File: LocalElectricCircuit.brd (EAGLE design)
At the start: 160 x 100 mm, 46 parts, among them IC1 PIC32MX360F512L, J1 Prog. Port, J3 Prog. Port, T1 PN100, U1 ADS1118, U2 ADS1118

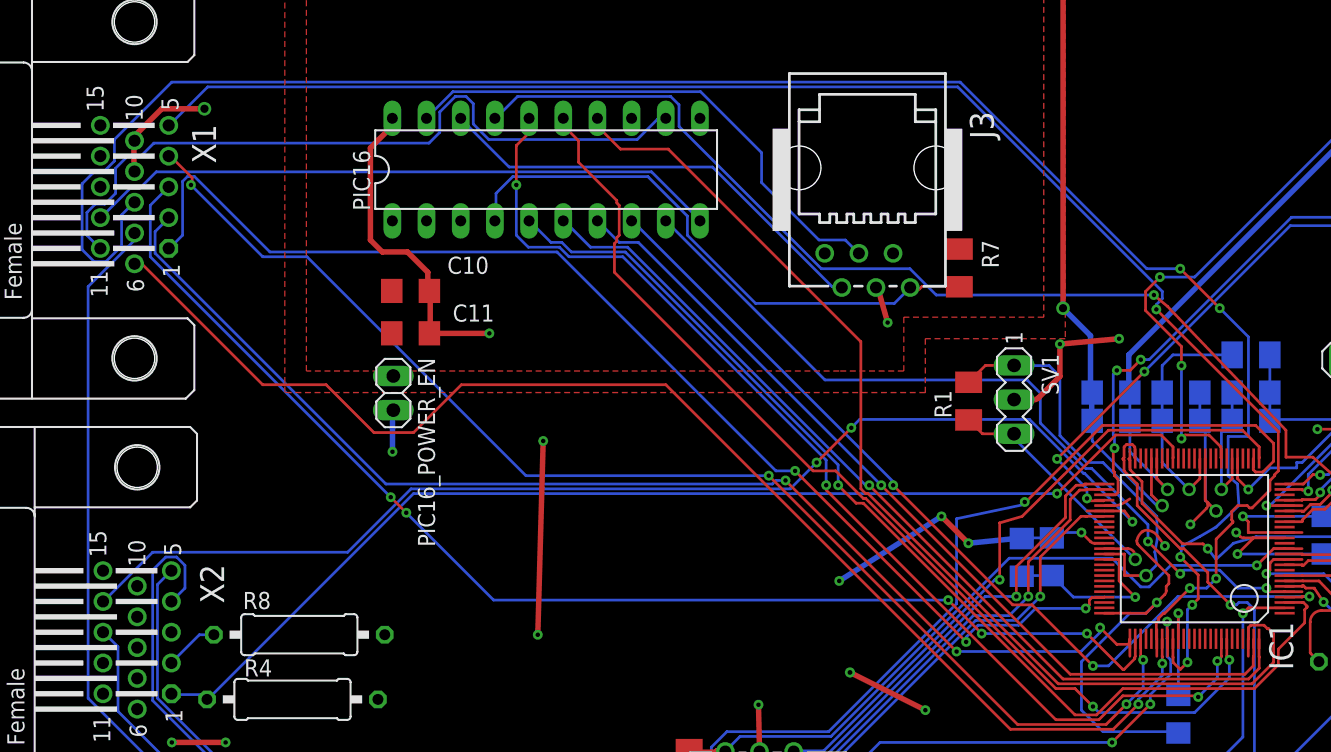
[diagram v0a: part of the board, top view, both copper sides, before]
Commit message: So far I've only ripped up a trace to have something to commit for the new branch
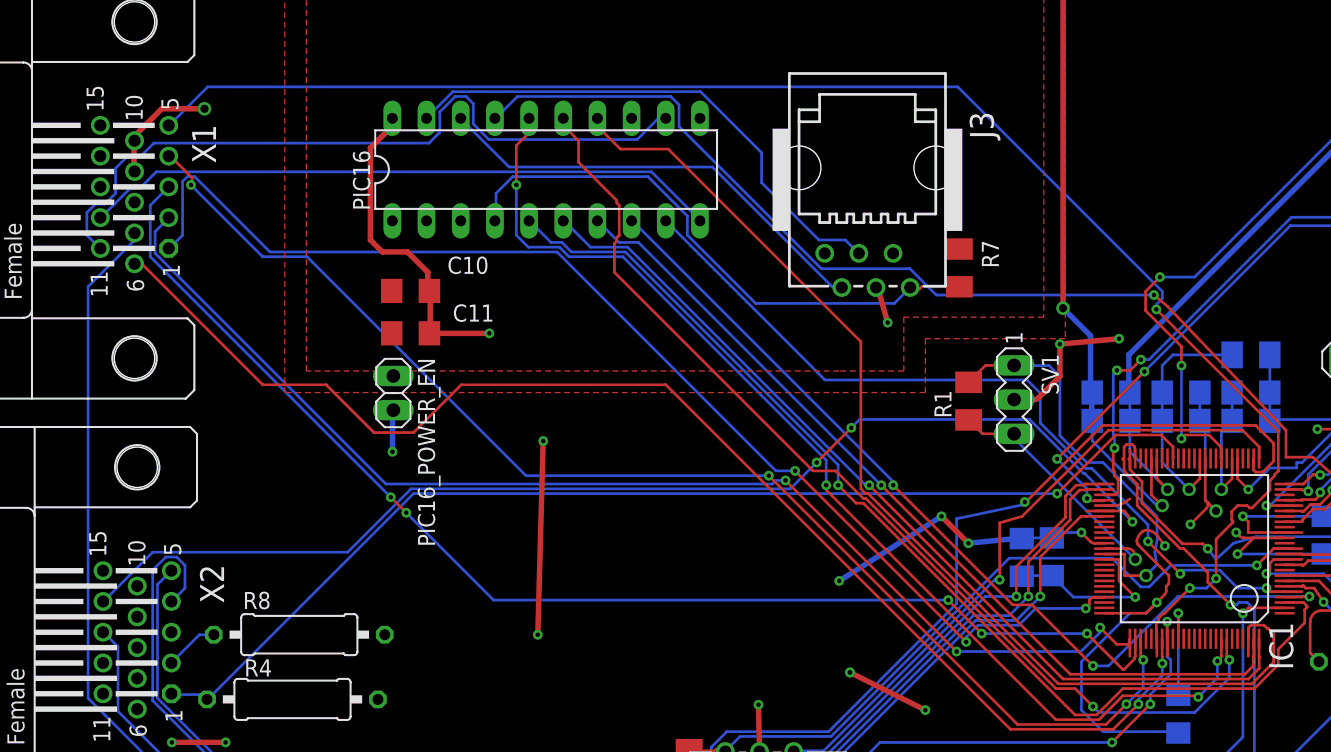
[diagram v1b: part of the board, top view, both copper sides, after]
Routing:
- net BALLC2: track 143.3 -> 0.00 mm, vias 5 -> 0
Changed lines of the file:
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@@
 <contactref element="IC1" pad="84"/>
 <contactref element="X1" pad="8"/>
-<wire x1="88.8" y1="-5.1" x2="88.8" y2="-6.4" width="0.2032" layer="1"/>
-<wire x1="88.8111" y1="-6.8453" x2="88.8111" y2="-6.4897" width="0.2032" layer="1"/>
-<wire x1="89.3445" y1="-7.3787" x2="88.8111" y2="-6.8453" width="0.2032" layer="1"/>
-<wire x1="89.8779" y1="-6.8453" x2="89.3445" y2="-7.3787" width="0.2032" layer="1"/>
-<wire x1="89.8779" y1="-2.9337" x2="89.8779" y2="-6.8453" width="0.2032" layer="16"/>
-<wire x1="90.2335" y1="-2.5781" x2="89.8779" y2="-2.9337" width="0.2032" layer="16"/>
-<wire x1="90.678" y1="-2.1336" x2="90.2335" y2="-2.5781" width="0.2032" layer="1"/>
-<wire x1="90.678" y1="-0.3556" x2="90.678" y2="-2.1336" width="0.2032" layer="1"/>
-<wire x1="89.3445" y1="0.9779" x2="90.678" y2="-0.3556" width="0.2032" layer="1"/>
-<wire x1="89.4779" y1="1.7779" x2="89.3445" y2="0.9779" width="0.2032" layer="16"/>
-<wire x1="93.7006" y1="4.8006" x2="92" y2="3.2" width="0.2032" layer="16"/>
-<wire x1="92" y1="3.2" x2="90.8" y2="2.5" width="0.2032" layer="16"/>
-<wire x1="90.8" y1="2.5" x2="89.4779" y2="1.7779" width="0.2032" layer="16"/>
-<wire x1="92.90431875" y1="9.934440625" x2="92.9" y2="7" width="0.2032" layer="16"/>
-<wire x1="92.9" y1="7" x2="93.6" y2="6.4" width="0.2032" layer="16"/>
-<wire x1="93.6" y1="6.4" x2="93.7006" y2="4.8006" width="0.2032" layer="16"/>
-<wire x1="94.4118" y1="9.936340625" x2="92.90431875" y2="9.934440625" width="0.2032" layer="16"/>
-<wire x1="94.4118" y1="17.3355" x2="94.4118" y2="9.936340625" width="0.2032" layer="16"/>
-<wire x1="92.2782" y1="19.4691" x2="94.4118" y2="17.3355" width="0.2032" layer="16"/>
-<wire x1="89.3445" y1="22.4028" x2="92.2782" y2="19.4691" width="0.2032" layer="1"/>
-<wire x1="86.8553" y1="22.4028" x2="89.3445" y2="22.4028" width="0.2032" layer="16"/>
-<wire x1="72.9869" y1="36.2712" x2="86.8553" y2="22.4028" width="0.2032" layer="16"/>
-<wire x1="14.4018" y1="36.2712" x2="72.9869" y2="36.2712" width="0.2032" layer="16"/>
-<wire x1="10.1346" y1="32.004" x2="14.4018" y2="36.2712" width="0.2032" layer="16"/>
-<wire x1="10.1346" y1="30.4038" x2="10.1346" y2="32.004" width="0.2032" layer="16"/>
-<wire x1="9.3345" y1="29.6037" x2="10.1346" y2="30.4038" width="0.2032" layer="16"/>
-<wire x1="8.6233" y1="29.6037" x2="9.3345" y2="29.6037" width="0.2032" layer="16"/>
-<wire x1="7.7343" y1="28.7147" x2="8.6233" y2="29.6037" width="0.2032" layer="16"/>
-<wire x1="7.7343" y1="23.8252" x2="7.7343" y2="28.7147" width="0.2032" layer="16"/>
-<wire x1="8.6233" y1="22.9362" x2="7.7343" y2="23.8252" width="0.2032" layer="16"/>
-<wire x1="9.5123" y1="22.9362" x2="8.6233" y2="22.9362" width="0.2032" layer="16"/>
-<wire x1="10.668" y1="24.0919" x2="9.5123" y2="22.9362" width="0.2032" layer="16"/>
-<wire x1="10.668" y1="26.4033" x2="10.668" y2="24.0919" width="0.2032" layer="16"/>
-<wire x1="11.557" y1="27.2923" x2="10.668" y2="26.4033" width="0.2032" layer="16"/>
-<wire x1="88.8111" y1="-6.4897" x2="88.8" y2="-6.4" width="0.2032" layer="1"/>
-<wire x1="11.557" y1="27.2923" x2="11.63" y2="27.342" width="0.2032" layer="16"/>
-<via x="89.8779" y="-6.8453" extent="1-16" drill="0.3302"/>
-<via x="90.2335" y="-2.5781" extent="1-16" drill="0.3302"/>
-<via x="89.3445" y="0.9779" extent="1-16" drill="0.3302"/>
-<via x="92.2782" y="19.4691" extent="1-16" drill="0.3302"/>
-<via x="89.3445" y="22.4028" extent="1-16" drill="0.3302"/>
+<wire x1="11.63" y1="27.342" x2="88.8" y2="-5.1" width="0" layer="19" extent="1-1"/>
 </signal>
 <signal name="BALLS1">

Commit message: Fan out step numero uno
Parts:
- removed PIC32_POWER_EN: (no value), pinhead:1X02
- moved C16 138.7 mm to (215.8, -26.2)
- moved C6 138.7 mm to (213.6, -26.3)
- moved C12 132.0 mm to (212.2, -21.3)
- moved C4 132.0 mm to (212.2, -19.2)
- moved C14 131.6 mm to (217.0, -21.3)
- moved C5 131.6 mm to (217.0, -19.2)
- moved C17 131.3 mm to (221.8, -21.3)
- moved C3 131.3 mm to (221.8, -19.2)
- moved R2 130.9 mm to (218.0, -27.8), turned to 270 degrees
- moved SV1 130.7 mm to (204.2, -17.3)
- moved IC1 130.7 mm to (217.6, -28.4)
- moved R1 130.7 mm to (200.8, -17.4)
- moved C1 128.1 mm to (217.4, -34.6)
- moved C15 128.1 mm to (217.4, -32.4)
- moved C7 126.8 mm to (214.0, -33.1)
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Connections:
- net +3V3: no longer PIC32_POWER_EN.1, PIC32_POWER_EN.2
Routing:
- net GND_3V3: track 258.8 -> 78.8 mm, vias 23 -> 6
- net BALLC1: track 131.4 -> 4.03 mm, vias 3 -> 1
- net U2TX: track 122.3 -> 0.00 mm, vias 3 -> 0
- net BALLA3: track 117.9 -> 3.70 mm, vias 3 -> 1
- net +3V3: track 197.4 -> 87.8 mm, vias 10 -> 6
- net U2RX: track 110.9 -> 4.03 mm, vias 1 -> 0
- net I_2_H: track 105.6 -> 4.90 mm, vias 3 -> 1
- net U1RX: track 102.4 -> 4.83 mm, vias 1 -> 0
- net BALLA4: track 98.2 -> 3.87 mm, vias 2 -> 1
- net BALLA2: track 95.3 -> 3.87 mm, vias 4 -> 1
- net GND_5V: track 91.3 -> 0.00 mm, vias 2 -> 0
- net U1TX: track 95.9 -> 4.67 mm, vias 1 -> 0
- net BALLS1: track 90.2 -> 0.00 mm, vias 3 -> 0
- net BALLA1: track 93.4 -> 3.70 mm, vias 5 -> 1
- net I2C_SCL: track 94.3 -> 5.66 mm, vias 1 -> 0
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- removed copper zone on layer 1, net +3V3
- removed copper zone on layer 16, net GND
- removed copper zone on layer 16, net GND_3V3
- removed copper zone on layer 16, net GND_5V
- removed copper zone on layer 1, net PIC16_3V3

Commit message: I'm a FAN of this pinout 😁 Am I right, laides 😉
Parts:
- moved C1 163.5 mm to (61.0, 13.0), turned to 90 degrees
- moved C2 162.1 mm to (65.8, 6.60), turned to 0 degrees
- moved C15 160.7 mm to (63.2, 13.0), turned to 90 degrees
- moved C13 160.4 mm to (65.8, 9.00), turned to 0 degrees
- moved C7 159.4 mm to (62.5, 16.4), turned to 0 degrees
- moved IC1 155.9 mm to (67.2, 12.8), turned to 0 degrees
- moved R2 155.5 mm to (67.8, 12.4), turned to 0 degrees
- moved C16 152.0 mm to (69.4, 14.6), turned to 0 degrees
- moved C6 150.5 mm to (69.3, 16.8), turned to 0 degrees
- moved C17 150.5 mm to (74.3, 8.60), turned to 90 degrees
- moved C3 148.0 mm to (76.4, 8.60), turned to 90 degrees
- moved C14 146.9 mm to (74.3, 13.4), turned to 270 degrees
- moved C5 144.3 mm to (76.4, 13.4), turned to 270 degrees
- moved C12 143.4 mm to (74.3, 18.2), turned to 270 degrees
- moved C4 140.9 mm to (76.4, 18.2), turned to 270 degrees
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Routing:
- net GND_3V3: track 78.8 -> 95.5 mm, vias 6 -> 11
- net OSC2: track 5.49 -> 22.0 mm, vias 0 -> 1
- net PIC16_3V3: track 0.00 -> 15.1 mm
- net OSC1: track 5.33 -> 20.4 mm, vias 0 -> 1
- net RB_TEMP: track 0.00 -> 6.10 mm, vias 0 -> 1
- net U2TX: track 0.00 -> 5.40 mm, vias 0 -> 1
- net N$12: track 4.10 -> 0.00 mm
- net N$11: track 4.10 -> 0.00 mm
- net I_1_L: track 8.03 -> 4.03 mm, vias 0 -> 1
- net PBUS7: track 8.03 -> 4.03 mm, vias 0 -> 1
- net PBUSC: track 7.87 -> 3.87 mm, vias 0 -> 1
- net PBUS5: track 8.36 -> 4.36 mm, vias 0 -> 1
- net TEMP_2: track 8.20 -> 4.20 mm, vias 0 -> 1
- net SDO2: track 8.20 -> 4.20 mm, vias 0 -> 1
- net CHARGE_PROBE_1: track 7.70 -> 3.70 mm, vias 0 -> 1
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
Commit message: Auto router did a goody
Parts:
- moved R1 0.41 mm to (74.5, 22.8)
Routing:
- net GND_3V3: track 95.5 -> 454.6 mm
- net +3V3: track 87.2 -> 416.7 mm
- net CHARGE_PROBE_0: track 4.67 -> 122.7 mm, vias 1 -> 2
- net TEMP_3: track 5.00 -> 122.0 mm, vias 1 -> 3
- net I2C_SCL: track 6.46 -> 114.6 mm
- net PIC16_TX: track 0.00 -> 106.2 mm
- net TEMP_2: track 4.20 -> 109.4 mm, vias 1 -> 3
- net U1RX: track 4.83 -> 107.4 mm, vias 1 -> 2
- net I2C_SDA: track 5.49 -> 107.5 mm
- net U2RX: track 4.43 -> 106.1 mm, vias 1 -> 2
- net I_1_L: track 4.03 -> 104.1 mm, vias 1 -> 4
- net CHARGE_PROBE_1: track 3.70 -> 102.5 mm, vias 1 -> 3
- net I_1_H: track 4.67 -> 103.2 mm, vias 1 -> 3
- net PIC16_RX: track 0.00 -> 98.3 mm
- net TEMP_1: track 5.16 -> 101.4 mm, vias 1 -> 4
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
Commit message: Power plane progress
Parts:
- removed R10, R9: 1k, rcl:0309/12
- removed T1: PN100, transistor:TO92
- moved R15 9.25 mm to (100.2, 0.40), turned to 0 degrees
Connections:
- removed net CONDUCTIVITY_ENABLE_3V: IC1.8, R15.2
- removed net CONDUCTIVITY_ENABLE_5V: J2.C14, R10.2, R9.1
- removed net N$10: R15.1, T1.1
- removed net N$5: R9.2, T1.3
- new net CONDUCTIVITY_ENABLE: IC1.8, J2.C14, R15.2
- net +3V3: now also R15.1
- net +5V: no longer T1.2
- net GND_5V: no longer R10.1
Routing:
- net CONDUCTIVITY_ENABLE: track 0.00 -> 100.1 mm, vias 0 -> 3
- net CONDUCTIVITY_ENABLE_3V: track 42.2 -> 0.00 mm, vias 2 -> 0
- net CONDUCTIVITY_ENABLE_5V: track 32.9 -> 0.00 mm
- net GND_5V: track 77.6 -> 65.6 mm
- net +5V: track 91.5 -> 80.4 mm
- net N$10: track 4.05 -> 0.00 mm
- net N$5: track 3.33 -> 0.00 mm
- added copper zone on layer 1, net +3V3
- added copper zone on layer 1, net +5V
- added copper zone on layer 16, net GND
- added copper zone on layer 16, net GND_3V3

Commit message: Tapping out
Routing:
- net +3V3: track 416.8 -> 493.2 mm
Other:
- board text added: "MALE"
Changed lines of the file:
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@@
 NorthWest Research Associates
 DigiPen Institute of Technology</text>
+<text x="1.5" y="7" size="1.778" layer="21">MALE</text>
 </plain>
 <attributes>
@@
 <wire x1="130.3274" y1="-30.4038" x2="130.405" y2="-30.417" width="0.4064" layer="16"/>
 <wire x1="152.1968" y1="38.4048" x2="152.1968" y2="39.2049" width="0.4064" layer="1"/>
-<wire x1="153.4414" y1="37.1602" x2="152.1968" y2="38.4048" width="0.4064" layer="1"/>
 <wire x1="153.4414" y1="16.0909" x2="153.4414" y2="37.1602" width="0.4064" layer="1"/>
 <wire x1="154.3304" y1="15.2019" x2="153.4414" y2="16.0909" width="0.4064" layer="1"/>
@@
 <vertex x="113.5" y="-14.5"/>
 </polygon>
+<wire x1="152.1968" y1="38.4048" x2="152.1968" y2="39.3032" width="0.6096" layer="1"/>
+<wire x1="152.1968" y1="39.3032" x2="152" y2="39.5" width="0.6096" layer="1"/>
+<wire x1="152" y1="39.5" x2="83.5" y2="39.5" width="0.6096" layer="1"/>
+<wire x1="83.5" y1="39.5" x2="79" y2="34.5" width="0.6096" layer="1"/>
+<wire x1="153.4414" y1="37.1602" x2="152.1968" y2="38.4048" width="0.4064" layer="1"/>
 </signal>
 <signal name="GND_3V3" class="1">

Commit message: 👌
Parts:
- added U$10, U$11, U$12, U$2, U$3, U$4, U$5, U$6, U$7, U$8, U$9: (no value), Logos:BALLOON
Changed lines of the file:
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@@
 <attribute name="VALUE" x="102.625" y="2.5142" size="1.27" layer="27" ratio="10"/>
 </element>
+<element name="U$2" library="Logos" package="BALLOON" value="" x="22.5" y="45"/>
+<element name="U$3" library="Logos" package="BALLOON" value="" x="68.1" y="9.9"/>
+<element name="U$4" library="Logos" package="BALLOON" value="" x="65.5" y="12.5"/>
+<element name="U$5" library="Logos" package="BALLOON" value="" x="67" y="14.2"/>
+<element name="U$6" library="Logos" package="BALLOON" value="" x="62.5" y="15"/>
+<element name="U$7" library="Logos" package="BALLOON" value="" x="70.1" y="17"/>
+<element name="U$8" library="Logos" package="BALLOON" value="" x="68.9" y="13.7"/>
+<element name="U$9" library="Logos" package="BALLOON" value="" x="64" y="17"/>
+<element name="U$10" library="Logos" package="BALLOON" value="" x="67.8" y="16.9"/>
+<element name="U$11" library="Logos" package="BALLOON" value="" x="62.8" y="12.1"/>
+<element name="U$12" library="Logos" package="BALLOON" value="" x="65.5" y="9.4"/>
 </elements>
 <signals>

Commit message: ⏚⏚⏚
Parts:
- removed J3: Prog. Port, con-amp:520258-3
- added JP1: (no value), pinhead:1X06
- moved R7 15.3 mm to (87.0, -34.4), turned to 180 degrees
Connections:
- net GND_3V3: now also JP1.3; no longer J3.3
- net PIC16_3V3: now also JP1.2; no longer J3.2
- net PIC16_MCLR: now also JP1.1; no longer J3.1
- net PIC16_PGC: now also JP1.5; no longer J3.5
- net PIC16_PGD: now also JP1.4; no longer J3.4
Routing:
- net +3V3: track 493.2 -> 555.2 mm, vias 10 -> 26
- net +3V1: track 0.00 -> 49.5 mm, vias 0 -> 6
- net +5V: track 80.4 -> 101.4 mm, vias 0 -> 6
- net PIC16_MCLR: track 40.8 -> 28.3 mm, vias 0 -> 1
- net PIC16_PGD: track 52.7 -> 40.2 mm
- net PIC16_3V3: track 63.7 -> 57.4 mm
- net PIC16_PGC: track 50.4 -> 55.4 mm
- net TEMP_1: track 101.4 -> 103.9 mm
- net I_1_L: track 104.1 -> 106.5 mm
- net TEMP_2: track 109.4 -> 111.4 mm
- net BALLS2: track 58.8 -> 60.6 mm
- net GND_3V3: track 454.6 -> 453.1 mm, vias 11 -> 45
- net PBUS0: track 38.9 -> 40.3 mm
